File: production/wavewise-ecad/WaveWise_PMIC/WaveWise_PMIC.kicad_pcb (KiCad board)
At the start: 4 copper layers, 43 parts, among them IC1 LV14360PDDAR, J12 Regulated 48V Input, J14 Battery Direct Input, J2 Inverter Inputs, J3 5031590300, J4 5031590400, J5 5031590400, J6 5031590400, J8 5031590800, K1 Relay_SPST-NO, Q2 2N2219, U1 Raspberry Pi Pico, U2 Pololu_DRV8711_Motor_Driver, U4 LM2576HVS-5.0_NOPB

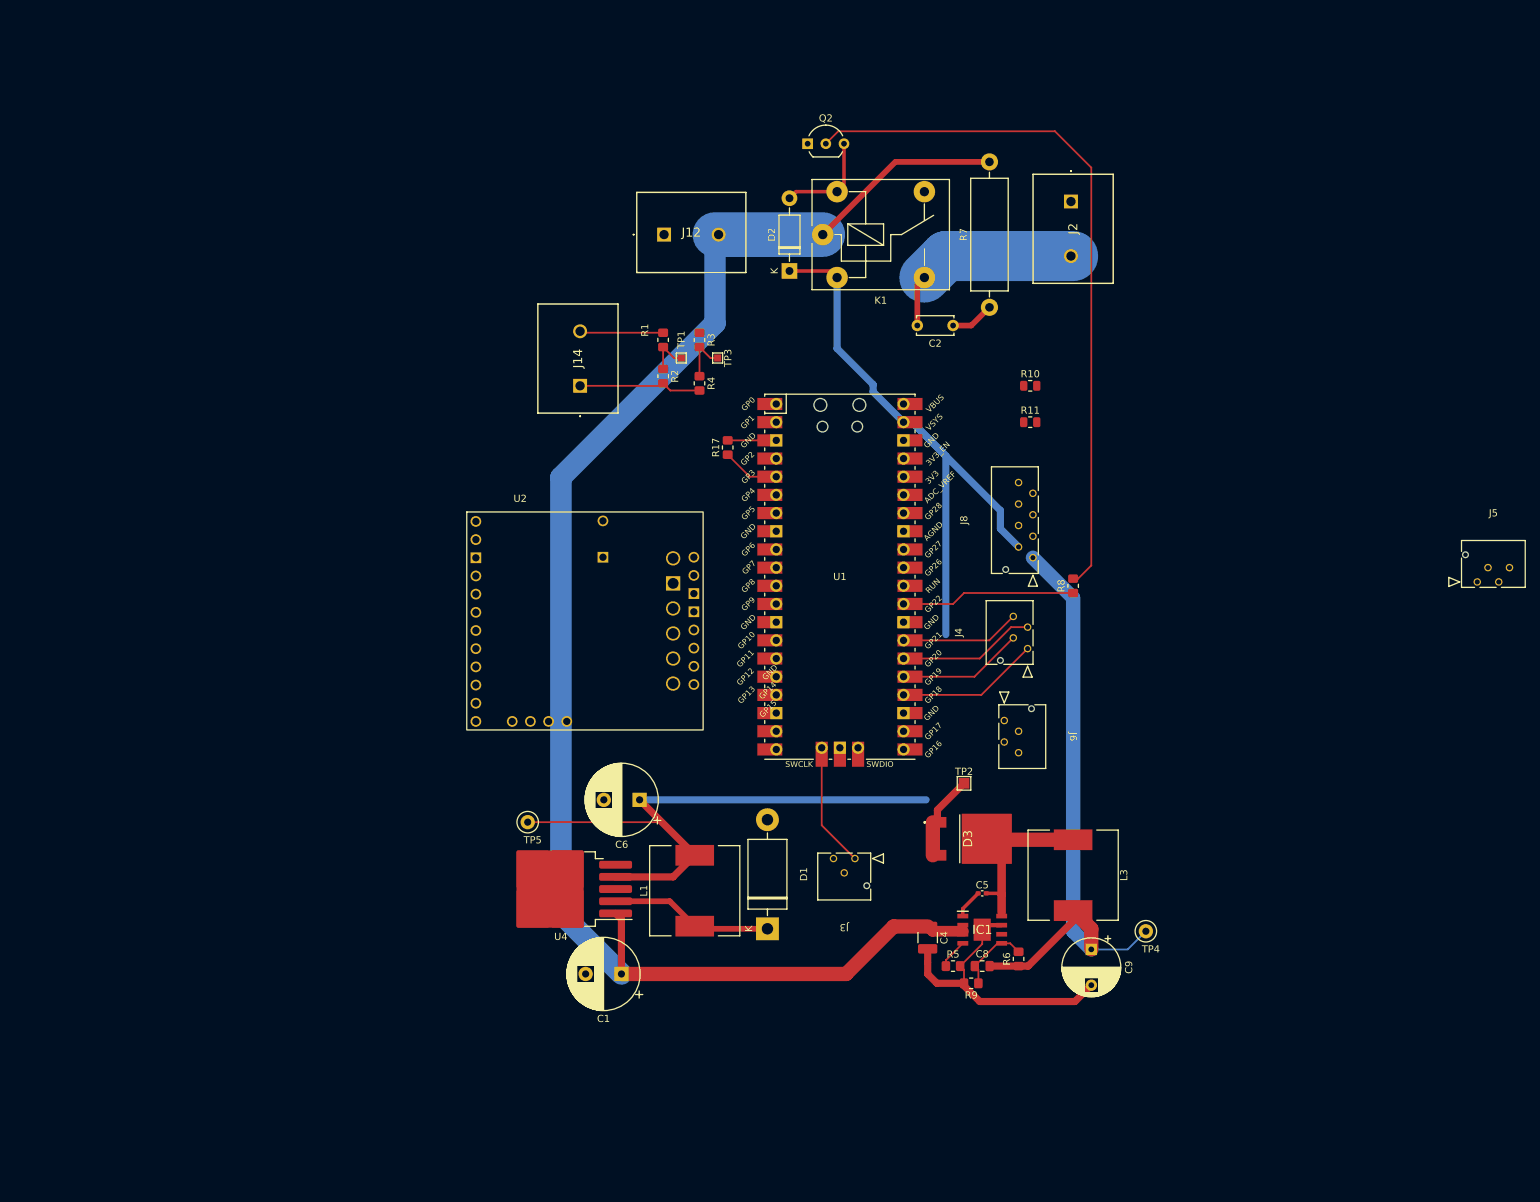
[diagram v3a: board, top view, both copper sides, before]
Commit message: Rearranged the whole board
All done aside from no place resistor and  power planes
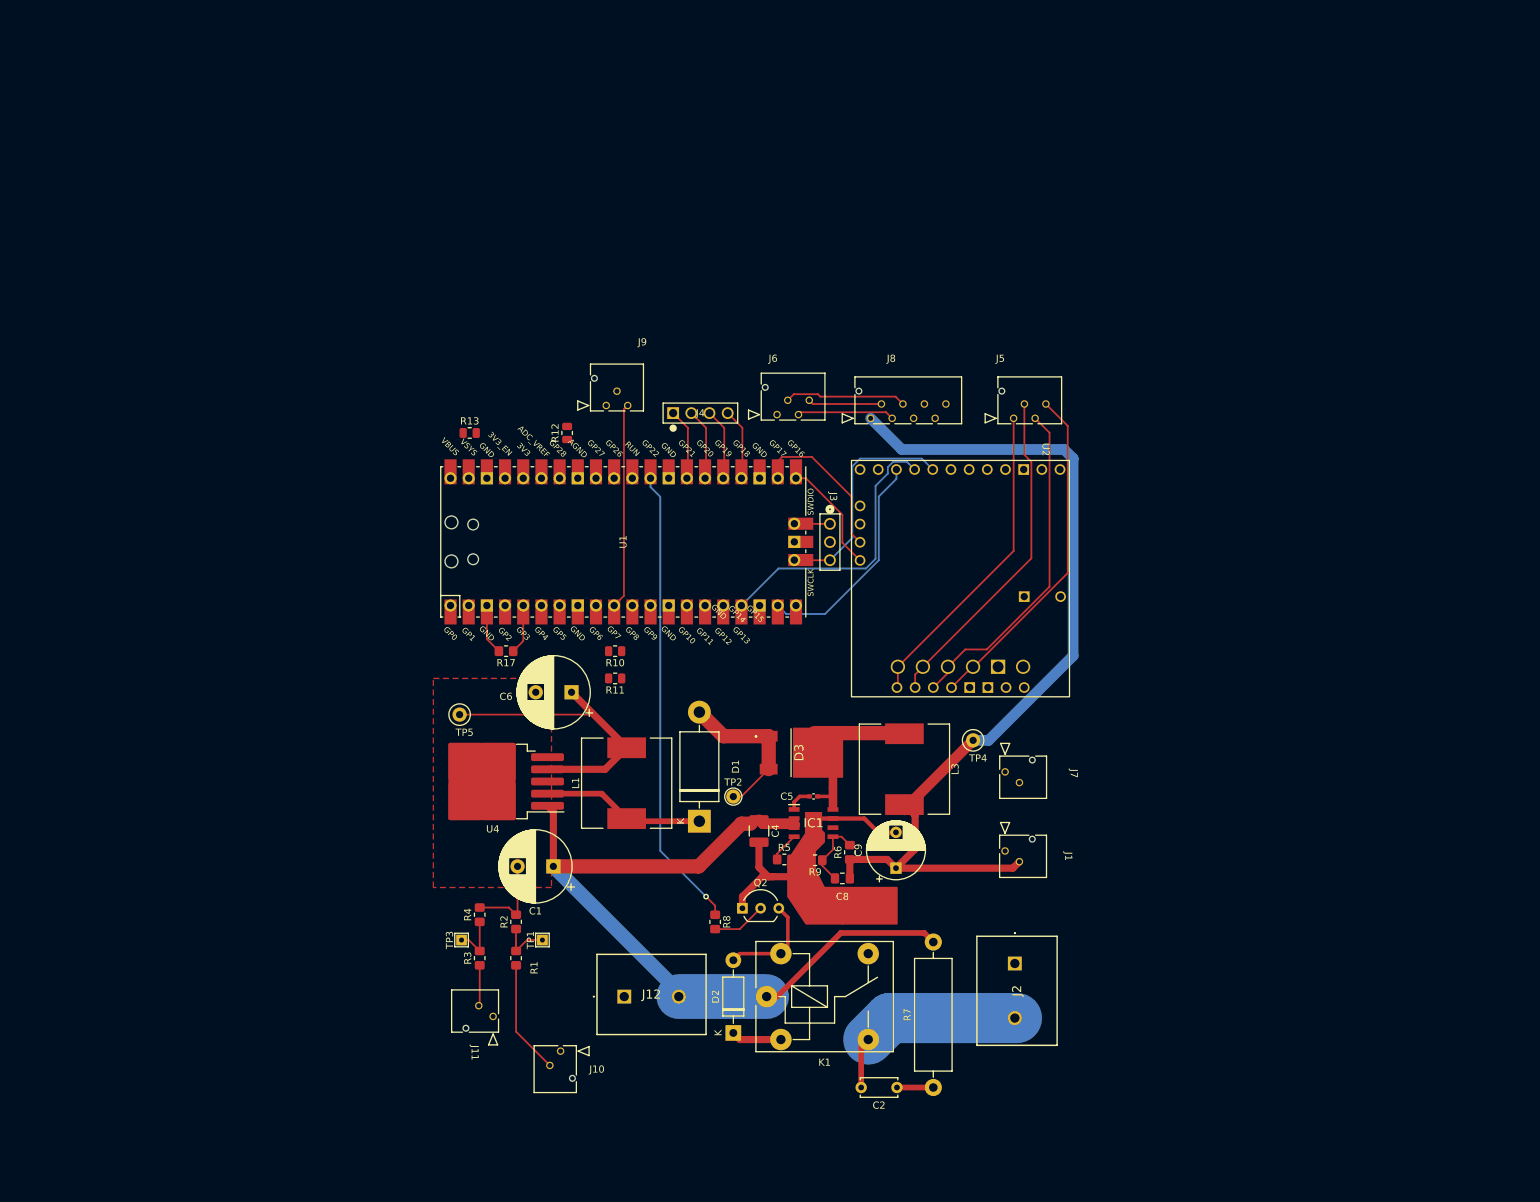
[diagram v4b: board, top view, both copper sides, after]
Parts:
- removed J14: Battery Direct Input, Unchecked:1731721
- added J1: 24V output, Unchecked:2pinmolex, F.Cu at (160.7, 131.0)
- added J10: 5031590200, Unchecked:2pinmolex, F.Cu at (98.6, 159.0)
- added J11: 5031590200, Unchecked:2pinmolex, F.Cu at (89.1, 154.1)
- added J7: 5V output, Unchecked:2pinmolex, F.Cu at (160.7, 120.0)
- added J9: 5031590300, Unchecked:3pinmolex, F.Cu at (105.0, 68.8)
- added R12: 0, Resistor_SMD:R_0805_2012Metric, F.Cu at (99.5, 72.6)
- added R13: 0, Resistor_SMD:R_0805_2012Metric, F.Cu at (85.9, 72.6)
- J3: value 5031590300 -> Conn_01x03_Pin; footprint Unchecked:3pinmolex -> Unchecked:61300311121
- J4: value 5031590400 -> Conn_01x04_Pin; footprint Footprints:4pinmolex -> Unchecked:61300411121
- TP1, TP3: footprint TestPoint:TestPoint_Pad_1.0x1.0mm -> TestPoint:TestPoint_THTPad_1.5x1.5mm_Drill0.7mm
- TP2: footprint TestPoint:TestPoint_Pad_1.5x1.5mm -> TestPoint:TestPoint_THTPad_D2.0mm_Drill1.0mm
- moved R7 109.3 mm to (150.6, 164.1)
- moved Q2 107.2 mm to (124.0, 139.0)
- moved C2 106.7 mm to (145.6, 164.1)
- moved D2 106.7 mm to (122.7, 156.4)
- moved K1 106.7 mm to (127.4, 151.4)
- moved J2 106.7 mm to (162.0, 146.7)
- moved J12 106.6 mm to (107.5, 151.4)
- moved R3 91.7 mm to (87.3, 146.0), turned to 90 degrees
- moved U2 89.6 mm to (172.1, 73.8), turned to -90 degrees
- moved TP3 88.8 mm to (84.7, 143.5), turned to 90 degrees
- moved R1 88.8 mm to (92.4, 146.0), turned to 90 degrees
- moved TP1 83.6 mm to (96.0, 143.5), turned to 90 degrees
- moved R4 80.3 mm to (87.3, 139.9), turned to 90 degrees
- moved R2 79.0 mm to (92.4, 140.9), turned to 90 degrees
- moved R10 68.8 mm to (106.2, 103.1), turned to 180 degrees
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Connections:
- C6 pad 2: (no net) -> GND
- C9 pad : (no net) -> +24V
- C9 pad 2: (no net) -> GND
- J3 pad 1: /CLK -> /Connectors/DIO
- J3 pad 3: /Connectors/DIO -> /CLK
- J4 pad 1: /GPIO1 -> /GPIO4
- J4 pad 2: /GPIO2 -> /GPIO3
- J4 pad 3: /GPIO3 -> /GPIO2
- J4 pad 4: /GPIO4 -> /GPIO1
- J5 pad 1: /Connectors/AOUT1 -> /Connectors/BOUT2
- J5 pad 2: /Connectors/AOUT2 -> /Connectors/BOUT1
- J5 pad 3: /Connectors/BOUT1 -> /Connectors/AOUT2
- J5 pad 4: /Connectors/BOUT2 -> /Connectors/AOUT1
- J6 pad 2: /Connectors/rockblock_RX_conn -> /Connectors/rockblock_RX
- J6 pad 3: /Connectors/rockblock_TX_conn -> /Connectors/rockblock_TX
- K1 pad 11: (no net) -> +48V
- U2 pad 1: +BATT -> +48V
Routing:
- net +48V: track 218.9 -> 109.0 mm
- net Net-(Q2-B): track 98.8 -> 7.56 mm
- net /Panel_Sense: track 7.24 -> 79.5 mm
- net /BATT_SENS: track 6.24 -> 77.6 mm
- net /MOTOR_FLT: track 0.00 -> 57.5 mm
- net /MOTOR_RESET: track 8.06 -> 64.4 mm
- net +5V: track 177.2 -> 122.8 mm
- net /Connectors/AOUT1: track 0.00 -> 47.7 mm
- net /Connectors/AOUT2: track 0.00 -> 46.9 mm
- net /Connectors/BOUT1: track 0.00 -> 46.7 mm
- net /Connectors/BOUT2: track 0.00 -> 44.4 mm
- net /PICO (BICO)/MOSI1: track 0.00 -> 42.9 mm
- net /PICO (BICO)/MISO1: track 0.00 -> 42.2 mm
- net +24V: track 89.0 -> 130.9 mm
- net /PUMP_CTL: track 24.3 -> 64.7 mm, vias 0 -> 1
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- added copper zone on F.Cu, net GND
- added copper zone on In2.Cu, net GND
- removed copper zone on In1.Cu, net GND

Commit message: Update WaveWise_PMIC.kicad_pcb
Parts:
- moved R10 1.70 mm to (104.5, 103.1)
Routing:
- net +5V: track 122.8 -> 173.0 mm
- net /CLK: track 31.7 -> 4.99 mm
- net /Connectors/Inverter_Input: track 29.1 -> 50.9 mm
- net +48V: track 109.0 -> 120.9 mm
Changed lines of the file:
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@@
   )
   (footprint "Resistor_SMD:R_0805_2012Metric" (layer "F.Cu")
-    (at 106.198594 103.107606 180)
+    (at 104.4975 103.107606 180)
     (descr "Resistor SMD 0805 (2012 Metric), square (rectangular) end terminal, IPC_7351 nominal, (Body size source: IPC-SM-782 page 72, https://www.pcb-3d.com/wordpress/wp-content/uploads/ipc-sm-782a_amendment_1_and_2.pdf), generated with kicad-footprint-generator")
     (tags "resistor")
@@
   (segment (start 97.565494 125.533806) (end 97.565494 133.178806) (width 1) (layer "F.Cu") (net 2))
   (segment (start 97.565494 133.178806) (end 117.875494 133.178806) (width 2) (layer "F.Cu") (net 2))
+  (segment (start 115.088594 151.367606) (end 126.985 151.367606) (width 6.25) (layer "In1.Cu") (net 2))
   (segment (start 115.088594 150.701906) (end 97.565494 133.178806) (width 2) (layer "B.Cu") (net 2))
   (segment (start 127.358594 151.367606) (end 115.088594 151.367606) (width 6.25) (layer "B.Cu") (net 2))
@@
   (segment (start 104.790494 119.618806) (end 107.805494 116.603806) (width 1) (layer "F.Cu") (net 9))
   (segment (start 143.400001 68.58) (end 133.831406 68.58) (width 0.25) (layer "F.Cu") (net 9))
+  (segment (start 133.35 149.86) (end 133.35 153.3762) (width 1) (layer "In1.Cu") (net 9))
+  (segment (start 133.35 153.3762) (end 129.358594 157.367606) (width 1) (layer "In1.Cu") (net 9))
+  (segment (start 162.680495 121.473805) (end 161.736195 121.473805) (width 1) (layer "In1.Cu") (net 9))
+  (segment (start 161.736195 121.473805) (end 133.35 149.86) (width 1) (layer "In1.Cu") (net 9))
   (segment (start 100.105494 108.853806) (end 100.105494 128.764506) (width 1) (layer "In2.Cu") (net 9))
   (segment (start 100.105494 128.764506) (end 122.708594 151.367606) (width 1) (layer "In2.Cu") (net 9))
@@
   (segment (start 140.568594 158.357606) (end 141.558594 157.367606) (width 0.25) (layer "F.Cu") (net 13))
   (segment (start 140.568594 164.067606) (end 140.568594 158.357606) (width 0.8) (layer "F.Cu") (net 13))
+  (segment (start 162.038594 154.367606) (end 144.558594 154.367606) (width 7) (layer "In1.Cu") (net 13))
+  (segment (start 144.558594 154.367606) (end 141.558594 157.367606) (width 7) (layer "In1.Cu") (net 13))
   (segment (start 144.558594 154.367606) (end 141.558594 157.367606) (width 7) (layer "B.Cu") (net 13))
   (segment (start 162.338594 154.367606) (end 144.558594 154.367606) (width 7) (layer "B.Cu") (net 13))
@@
   (segment (start 92.358594 144.997606) (end 92.358594 141.927606) (width 0.25) (layer "F.Cu") (net 16))
   (segment (start 93.888594 143.467606) (end 92.358594 144.997606) (width 0.25) (layer "F.Cu") (net 16))
-  (segment (start 102.345494 137.160706) (end 102.345494 82.668806) (width 0.25) (layer "In1.Cu") (net 16))
-  (segment (start 102.345494 82.668806) (end 106.060494 78.953806) (width 0.25) (layer "In1.Cu") (net 16))
-  (segment (start 96.038594 143.467606) (end 102.345494 137.160706) (width 0.25) (layer "In1.Cu") (net 16))
+  (segment (start 99.615494 85.398806) (end 106.060494 78.953806) (width 0.25) (layer "B.Cu") (net 16))
+  (segment (start 96.038594 143.467606) (end 96.038594 109.794539) (width 0.25) (layer "B.Cu") (net 16))
+  (segment (start 99.615494 106.217639) (end 99.615494 85.398806) (width 0.25) (layer "B.Cu") (net 16))
+  (segment (start 96.038594 109.794539) (end 99.615494 106.217639) (width 0.25) (layer "B.Cu") (net 16))
   (segment (start 87.278594 152.507606) (end 87.148594 152.637606) (width 0.25) (layer "F.Cu") (net 17))
   (segment (start 87.278594 146.997606) (end 87.278594 152.507606) (width 0.25) (layer "F.Cu") (net 17))
@@
   (segment (start 85.748594 143.467606) (end 87.278594 144.997606) (width 0.25) (layer "F.Cu") (net 18))
   (segment (start 84.738594 143.467606) (end 85.748594 143.467606) (width 0.25) (layer "F.Cu") (net 18))
-  (segment (start 89.645494 92.828806) (end 89.645494 138.560706) (width 0.25) (layer "In2.Cu") (net 18))
-  (segment (start 89.645494 138.560706) (end 84.738594 143.467606) (width 0.25) (layer "In2.Cu") (net 18))
-  (segment (start 103.520494 78.953806) (end 89.645494 92.828806) (width 0.25) (layer "In2.Cu") (net 18))
+  (segment (start 89.645494 138.560706) (end 84.738594 143.467606) (width 0.25) (layer "B.Cu") (net 18))
+  (segment (start 103.520494 78.953806) (end 89.645494 92.828806) (width 0.25) (layer "B.Cu") (net 18))
+  (segment (start 89.645494 92.828806) (end 89.645494 138.560706) (width 0.25) (layer "B.Cu") (net 18))
   (segment (start 93.360494 101.705706) (end 93.360494 96.733806) (width 0.25) (layer "F.Cu") (net 19))
   (segment (start 91.958594 103.107606) (end 93.360494 101.705706) (width 0.25) (layer "F.Cu") (net 19))
@@
   (segment (start 131.254294 90.407606) (end 136.208694 90.407606) (width 0.25) (layer "F.Cu") (net 26))
   (segment (start 131.230494 90.383806) (end 131.254294 90.407606) (width 0.25) (layer "F.Cu") (net 26))
-  (segment (start 139.337394 77.287726) (end 140.417114 76.208006) (width 0.25) (layer "B.Cu") (net 26))
-  (segment (start 139.337394 87.278906) (end 139.337394 77.287726) (width 0.25) (layer "B.Cu") (net 26))
-  (segment (start 149.047394 76.208006) (end 150.572394 77.733006) (width 0.25) (layer "B.Cu") (net 26))
-  (segment (start 136.208694 90.407606) (end 139.337394 87.278906) (width 0.25) (layer "B.Cu") (net 26))
-  (segment (start 140.417114 76.208006) (end 149.047394 76.208006) (width 0.25) (layer "B.Cu") (net 26))
   (segment (start 131.230494 85.303806) (end 131.254294 85.327606) (width 0.25) (layer "F.Cu") (net 27))
   (segment (start 131.254294 85.327606) (end 136.208694 85.327606) (width 0.25) (layer "F.Cu") (net 27))
@@
   (segment (start 144.05 69.730001) (end 132.146614 69.730001) (width 0.25) (layer "F.Cu") (net 36))
   (segment (start 132.146614 69.730001) (end 131.814009 70.062606) (width 0.25) (layer "F.Cu") (net 36))
+  (segment (start 145.375003 67.555001) (end 134.865001 67.555001) (width 0.25) (layer "F.Cu") (net 37))
   (segment (start 146.400002 68.58) (end 145.375003 67.555001) (width 0.25) (layer "F.Cu") (net 37))
-  (segment (start 145.375003 67.555001) (end 134.865001 67.555001) (width 0.25) (layer "F.Cu") (net 37))
+  (segment (start 134.522605 67.212605) (end 131.16401 67.212605) (width 0.25) (layer "F.Cu") (net 37))
+  (segment (start 131.16401 67.212605) (end 130.31401 68.062605) (width 0.25) (layer "F.Cu") (net 37))
   (segment (start 134.865001 67.555001) (end 134.522605 67.212605) (width 0.25) (layer "F.Cu") (net 37))
-  (segment (start 131.16401 67.212605) (end 130.31401 68.062605) (width 0.25) (layer "F.Cu") (net 37))
-  (segment (start 134.522605 67.212605) (end 131.16401 67.212605) (width 0.25) (layer "F.Cu") (net 37))
   (segment (start 140.412394 77.733006) (end 138.016594 80.128806) (width 0.25) (layer "In2.Cu") (net 41))
   (segment (start 107.425494 80.128806) (end 90.820494 96.733806) (width 0.25) (layer "In2.Cu") (net 41))
   (segment (start 138.016594 80.128806) (end 107.425494 80.128806) (width 0.25) (layer "In2.Cu") (net 41))
-  (segment (start 107.425494 69.319713) (end 107.425494 95.368806) (width 0.25) (layer "F.Cu") (net 44))
-  (segment (start 107.952601 68.792606) (end 107.425494 69.319713) (width 0.25) (layer "F.Cu") (net 44))
-  (segment (start 107.425494 95.368806) (end 106.060494 96.733806) (width 0.25) (layer "F.Cu") (net 44))
+  (segment (start 107.425494 95.368806) (end 106.060494 96.733806) (width 0.25) (layer "B.Cu") (net 44))
+  (segment (start 107.952601 68.792606) (end 107.425494 69.319713) (width 0.25) (layer "B.Cu") (net 44))
+  (segment (start 107.425494 69.319713) (end 107.425494 95.368806) (width 0.25) (layer "B.Cu") (net 44))
   (segment (start 118.760494 96.733806) (end 118.760494 95.625706) (width 0.25) (layer "In2.Cu") (net 47))
   (segment (start 142.51379 78.808006) (end 152.037394 78.808006) (width 0.25) (layer "In2.Cu") (net 47))

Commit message: more change
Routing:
- net /CLK: track 4.99 -> 25.5 mm
- net /PICO (BICO)/SCS: track 39.5 -> 37.7 mm
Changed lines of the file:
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@@
   (segment (start 131.254294 90.407606) (end 136.208694 90.407606) (width 0.25) (layer "F.Cu") (net 26))
   (segment (start 131.230494 90.383806) (end 131.254294 90.407606) (width 0.25) (layer "F.Cu") (net 26))
+  (segment (start 137.648294 88.968006) (end 136.208694 90.407606) (width 0.25) (layer "B.Cu") (net 26))
+  (segment (start 150.572394 77.733006) (end 150.572394 79.253286) (width 0.25) (layer "B.Cu") (net 26))
+  (segment (start 150.572394 79.253286) (end 140.857674 88.968006) (width 0.25) (layer "B.Cu") (net 26))
+  (segment (start 140.857674 88.968006) (end 137.648294 88.968006) (width 0.25) (layer "B.Cu") (net 26))
   (segment (start 131.230494 85.303806) (end 131.254294 85.327606) (width 0.25) (layer "F.Cu") (net 27))
   (segment (start 131.254294 85.327606) (end 136.208694 85.327606) (width 0.25) (layer "F.Cu") (net 27))
@@
   (segment (start 144.247794 89.137606) (end 128.896694 89.137606) (width 0.25) (layer "In1.Cu") (net 48))
   (segment (start 128.896694 89.137606) (end 121.300494 96.733806) (width 0.25) (layer "In1.Cu") (net 48))
-  (segment (start 141.240998 91.558806) (end 142.578594 90.22121) (width 0.25) (layer "B.Cu") (net 49))
+  (segment (start 144.298594 77.406526) (end 145.047114 76.658006) (width 0.25) (layer "B.Cu") (net 49))
+  (segment (start 146.957394 76.658006) (end 148.032394 77.733006) (width 0.25) (layer "B.Cu") (net 49))
   (segment (start 142.578594 80.017086) (end 144.298594 78.297086) (width 0.25) (layer "B.Cu") (net 49))
+  (segment (start 129.015494 91.558806) (end 129.015494 84.344506) (width 0.25) (layer "B.Cu") (net 49))
   (segment (start 144.298594 78.297086) (end 144.298594 77.406526) (width 0.25) (layer "B.Cu") (net 49))
+  (segment (start 129.015494 84.344506) (end 133.342914 80.017086) (width 0.25) (layer "B.Cu") (net 49))
   (segment (start 145.047114 76.658006) (end 146.957394 76.658006) (width 0.25) (layer "B.Cu") (net 49))
   (segment (start 123.840494 96.733806) (end 129.015494 91.558806) (width 0.25) (layer "B.Cu") (net 49))
-  (segment (start 146.957394 76.658006) (end 148.032394 77.733006) (width 0.25) (layer "B.Cu") (net 49))
-  (segment (start 129.015494 91.558806) (end 141.240998 91.558806) (width 0.25) (layer "B.Cu") (net 49))
-  (segment (start 142.578594 90.22121) (end 142.578594 80.017086) (width 0.25) (layer "B.Cu") (net 49))
-  (segment (start 144.298594 77.406526) (end 145.047114 76.658006) (width 0.25) (layer "B.Cu") (net 49))
-  (segment (start 130.095494 97.908806) (end 128.920494 96.733806) (width 0.25) (layer "B.Cu") (net 50))
-  (segment (start 135.527394 97.908806) (end 130.095494 97.908806) (width 0.25) (layer "B.Cu") (net 50))
+  (segment (start 133.342914 80.017086) (end 142.578594 80.017086) (width 0.25) (layer "B.Cu") (net 49))
+  (segment (start 130.055494 84.574506) (end 130.055494 95.598806) (width 0.25) (layer "B.Cu") (net 50))
+  (segment (start 143.028594 81.517606) (end 133.112394 81.517606) (width 0.25) (layer "B.Cu") (net 50))
   (segment (start 145.492394 77.733006) (end 145.492394 79.053806) (width 0.25) (layer "B.Cu") (net 50))
-  (segment (start 143.028594 81.517606) (end 143.028594 90.407606) (width 0.25) (layer "B.Cu") (net 50))
-  (segment (start 143.028594 90.407606) (end 135.527394 97.908806) (width 0.25) (layer "B.Cu") (net 50))
   (segment (start 145.492394 79.053806) (end 143.028594 81.517606) (width 0.25) (layer "B.Cu") (net 50))
+  (segment (start 130.055494 95.598806) (end 128.920494 96.733806) (width 0.25) (layer "B.Cu") (net 50))
+  (segment (start 133.112394 81.517606) (end 130.055494 84.574506) (width 0.25) (layer "B.Cu") (net 50))
   (segment (start 132.844794 78.953806) (end 131.460494 78.953806) (width 0.25) (layer "F.Cu") (net 52))
   (segment (start 140.412394 90.433006) (end 137.948594 87.969206) (width 0.25) (layer "F.Cu") (net 52))
